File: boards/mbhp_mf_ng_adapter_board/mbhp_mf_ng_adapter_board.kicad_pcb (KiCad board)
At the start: 2 copper layers, 76.2 x 35.6 mm, 12 parts, among them J1 Analog Inputs, J2 Power, U1 NodeMCU_ESP32, U2 MCP3208, U3 PIC18FAdapter

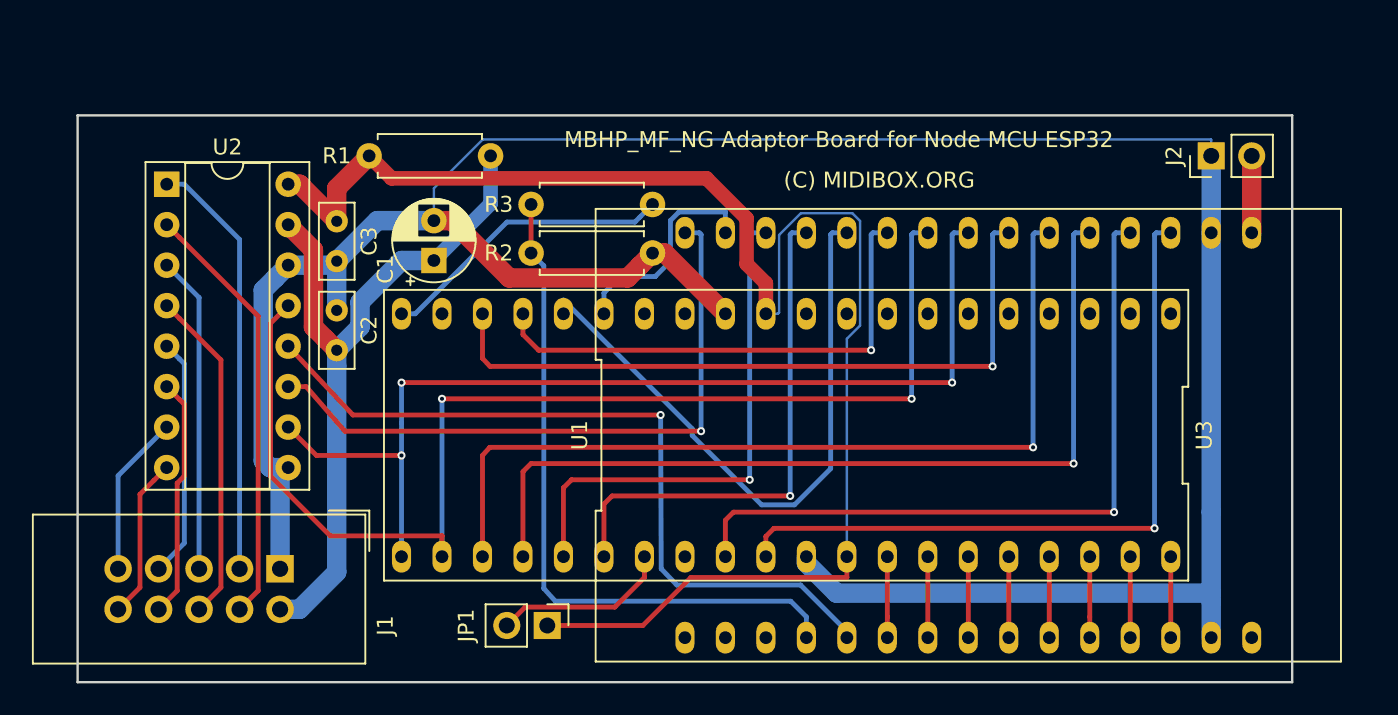
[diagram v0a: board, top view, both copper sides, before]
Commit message: Adaptor prototype ready for OSHpark
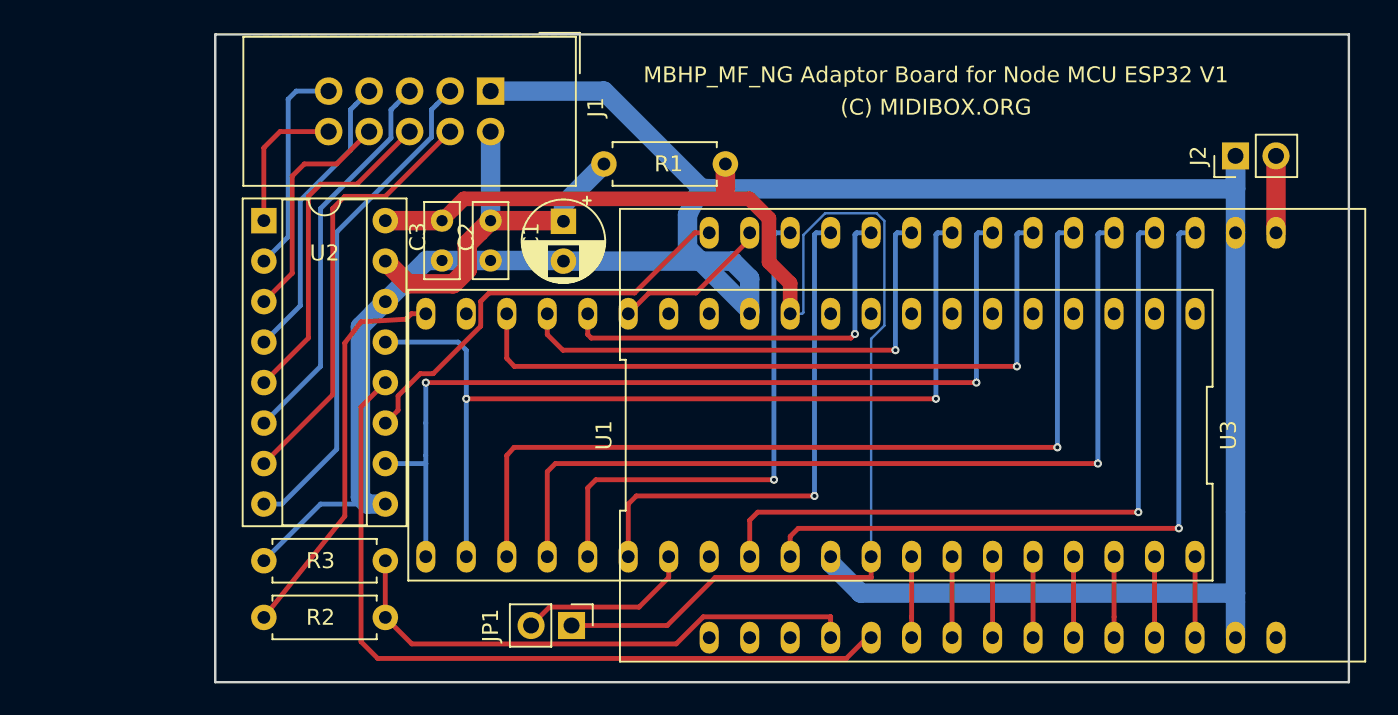
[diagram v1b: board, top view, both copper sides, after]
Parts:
- moved J1 32.8 mm to (132.6, 64.5)
- moved R3 31.1 mm to (118.4, 94.0), turned to 0 degrees
- moved R2 27.5 mm to (126.0, 97.5), turned to 180 degrees
- moved R1 22.4 mm to (147.3, 69.1), turned to 180 degrees
- moved C2 12.6 mm to (132.6, 72.6), turned to 270 degrees
- moved C1 8.49 mm to (137.2, 72.7), turned to 270 degrees
- moved C3 6.60 mm to (129.5, 75.1)
- moved U2 6.51 mm to (118.4, 72.6)
- moved J2 1.52 mm to (179.3, 68.6)
- moved JP1 1.52 mm to (137.7, 98.0)
- moved U1 1.52 mm to (164.1, 86.1)
- moved U3 1.52 mm to (152.7, 86.1)
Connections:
- U2 pad 1: Net-(J1-Pad3) -> Net-(J1-Pad10)
- U2 pad 2: Net-(J1-Pad4) -> Net-(J1-Pad9)
- U2 pad 3: Net-(J1-Pad5) -> Net-(J1-Pad8)
- U2 pad 4: Net-(J1-Pad6) -> Net-(J1-Pad7)
- U2 pad 5: Net-(J1-Pad7) -> Net-(J1-Pad6)
- U2 pad 6: Net-(J1-Pad8) -> Net-(J1-Pad5)
- U2 pad 7: Net-(J1-Pad9) -> Net-(J1-Pad4)
- U2 pad 8: Net-(J1-Pad10) -> Net-(J1-Pad3)
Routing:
- net Net-(C1-Pad1): track 45.0 -> 24.6 mm
- net /SPI_CLK: track 75.5 -> 59.1 mm
- net Net-(U1-Pad26): track 39.9 -> 25.6 mm, vias 0 -> 1
- net /SPI_MOSI: track 40.6 -> 26.7 mm, vias 1 -> 0
- net /SPI_MISO_DINSR: track 43.0 -> 34.2 mm
- net Net-(R2-Pad2): track 18.6 -> 24.9 mm
- net +5V: track 95.1 -> 89.3 mm
- net /SPI_CS: track 63.7 -> 58.4 mm, vias 3 -> 2
- net Net-(J1-Pad3): track 26.7 -> 31.4 mm
- net Net-(J1-Pad5): track 19.9 -> 24.6 mm
- net Net-(U1-Pad29): track 13.8 -> 9.96 mm
- net Net-(J1-Pad9): track 10.2 -> 13.5 mm
- net Net-(J1-Pad7): track 15.1 -> 18.5 mm
- net GNDA: track 166.5 -> 168.2 mm
- net /SPI_MISO_ADC: track 48.6 -> 49.9 mm, vias 1 -> 0
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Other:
- board size 76.2 x 35.6 mm -> 71.1 x 40.6 mm
- board text added: "MBHP_MF_NG Adaptor Board for Node MCU ESP32 V1"
- board text removed: "MBHP_MF_NG Adaptor Board for Node MCU ESP32"
